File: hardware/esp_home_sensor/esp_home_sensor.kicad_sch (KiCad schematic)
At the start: 0 parts

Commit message: schematic
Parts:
- added BT1: Battery_Cell, symbol Device:Battery_Cell
- added J2, J3: Conn_01x04_MountingPin, Connector_JST:JST_SH_SM04B-SRSS-TB_1x04-1MP_P1.00mm_Horizontal, symbol Connector_Generic_MountingPin:Conn_01x04_MountingPin
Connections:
- new net 3V3_AUX: J2.3 (Pin_3), J3.3 (Pin_3)
- new net Env_sensor/SCL: J2.1 (Pin_1), J3.1 (Pin_1)
- new net Env_sensor/SDA: J2.2 (Pin_2), J3.2 (Pin_2)
- new net GND: J2.4 (Pin_4), J3.4 (Pin_4)
- new net Protection/BAT+: BT1.1 (+)
- new net Protection/BAT-: BT1.2 (-)
- no-connect marks 0 -> 2
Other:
- added sheet Charger (charger.kicad_sch)
- added sheet Env_sensor (env_sensor.kicad_sch)
- added sheet LDO (LDO.kicad_sch)
- added sheet Light_sensor (light_sensor.kicad_sch)
- added sheet MCU (MCU.kicad_sch)
- added sheet Protection (protection.kicad_sch)
- added sheet USB (USB.kicad_sch)

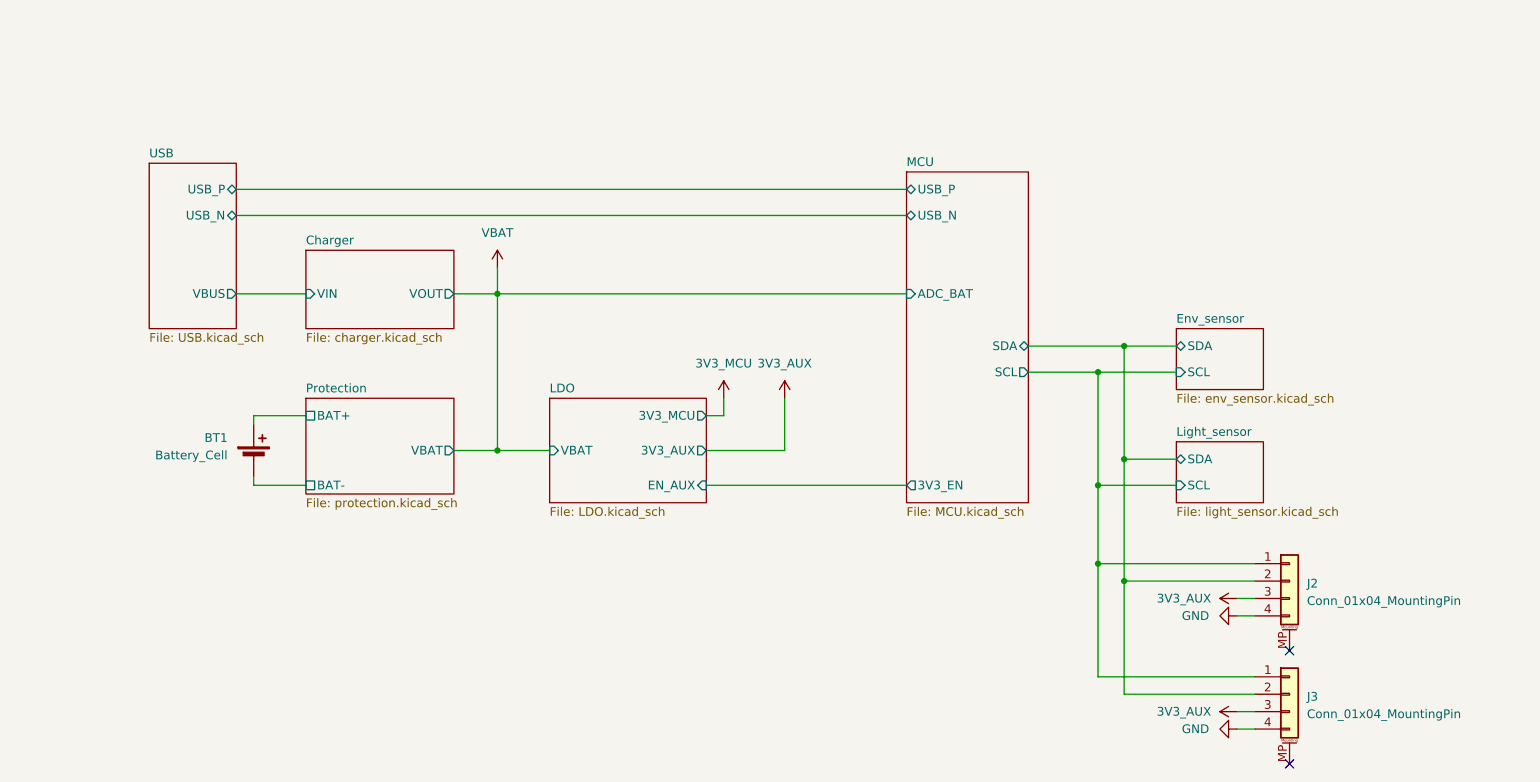
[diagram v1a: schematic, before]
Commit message: busses, display connector, footprint lib
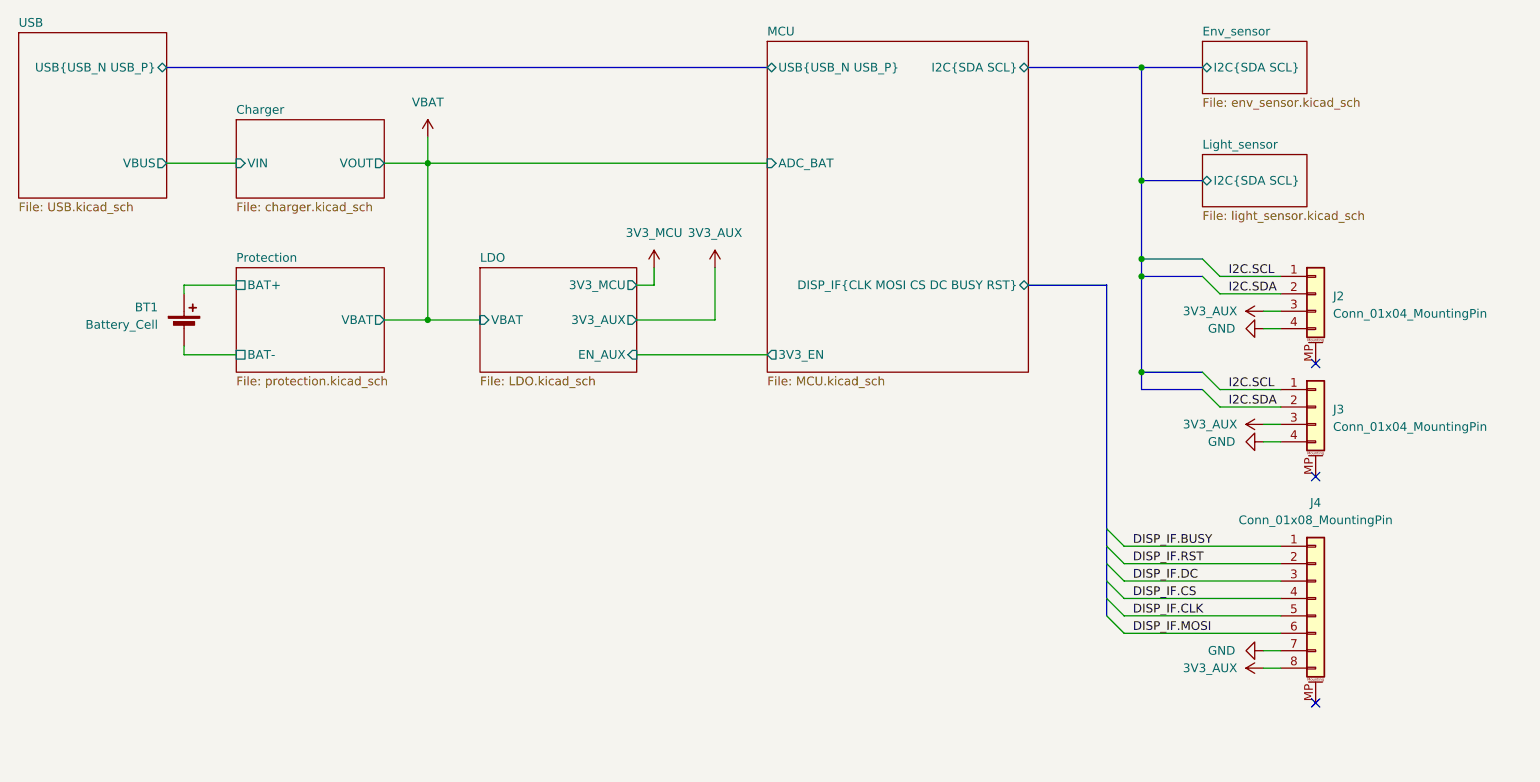
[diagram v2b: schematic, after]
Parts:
- added J4: Conn_01x08_MountingPin, Connector_JST:JST_SH_SM08B-SRSS-TB_1x08-1MP_P1.00mm_Horizontal, symbol Connector_Generic_MountingPin:Conn_01x08_MountingPin
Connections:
- net 3V3_AUX: now also J4.8 (Pin_8)
- net GND: now also J4.7 (Pin_7)
- net Env_sensor/SCL renamed I2C.SCL
- net Env_sensor/SDA renamed I2C.SDA
- new net DISP_IF.BUSY: J4.1 (Pin_1)
- new net DISP_IF.CLK: J4.5 (Pin_5)
- new net DISP_IF.CS: J4.4 (Pin_4)
- new net DISP_IF.DC: J4.3 (Pin_3)
- new net DISP_IF.MOSI: J4.6 (Pin_6)
- new net DISP_IF.RST: J4.2 (Pin_2)
- no-connect marks 2 -> 3
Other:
- sheet Env_sensor ports: added I2C{SDA SCL}; removed SCL, SDA
- sheet Light_sensor ports: added I2C{SDA SCL}; removed SCL, SDA
- sheet MCU ports: added DISP_IF{CLK MOSI CS DC BUSY RST}, I2C{SDA SCL}, USB{USB_N USB_P}; removed SCL, SDA, USB_N, USB_P
- sheet USB ports: added USB{USB_N USB_P}; removed USB_N, USB_P
- moved on the sheet: BT1, J2, J3

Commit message: footprint assignment, buck
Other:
- sheet LDO renamed DC_DC
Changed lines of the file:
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@@
+			)
+		)
+		(property "Mfr. No." ""
+			(at 218.44 99.06 0)
+			(hide yes)
+			(show_name no)
+			(do_not_autoplace no)
+			(effects
+				(font
+					(size 1.27 1.27)
+				)
 			)
 		)
@@
 			)
 		)
+		(property "Mfr. No." ""
+			(at 218.44 82.55 0)
+			(hide yes)
+			(show_name no)
+			(do_not_autoplace no)
+			(effects
+				(font
+					(size 1.27 1.27)
+				)
+			)
+		)
 		(pin "MP"
 		)
@@
 			)
 		)
+		(property "Mfr. No." ""
+			(at 53.34 87.63 0)
+			(hide yes)
+			(show_name no)
+			(do_not_autoplace no)
+			(effects
+				(font
+					(size 1.27 1.27)
+				)
+			)
+		)
 		(pin "1"
 		)
@@
 			)
 		)
+		(property "Mfr. No." ""
+			(at 218.44 127 0)
+			(hide yes)
+			(show_name no)
+			(do_not_autoplace no)
+			(effects
+				(font
+					(size 1.27 1.27)
+				)
+			)
+		)
 		(pin "7"
 		)
@@
 			(color 0 0 0 0)
 		)
-		(property "Sheetname" "LDO"
+		(property "Sheetname" "DC_DC"
 			(at 96.52 78.0284 0)
 			(show_name no)

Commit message: minor update
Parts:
- BT1: footprint (none) -> Battery:BatteryHolder_Keystone_1042_1x18650
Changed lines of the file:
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@@
 			)
 		)
-		(property "Footprint" ""
+		(property "Footprint" "Battery:BatteryHolder_Keystone_1042_1x18650"
 			(at 53.34 86.106 90)
 			(hide yes)

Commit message: initial layout, power routing
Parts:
- added H1, H2, H3, H4: MountingHole, MountingHole:MountingHole_2.2mm_M2, symbol Mechanical:MountingHole
- added R18: 100, Resistor_SMD:R_0402_1005Metric, symbol Device:R
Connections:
- net VBAT: now also R18.2
- new net MCU/ADC_BAT: R18.1

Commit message: layout
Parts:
- added TP24, TP25, TP27, TP28, TP29, TP30: TestPoint, TestPoint:TestPoint_Pad_D2.5mm, symbol Connector:TestPoint
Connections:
- net 3V3_AUX: now also TP25.1
- net 3V3_MCU: now also TP27.1
- net GND: now also TP24.1, TP29.1, TP30.1
- net VBAT: now also TP28.1

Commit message: layout
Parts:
- renumbered J2 to J1, J3 to J2, J4 to J3, R18 to R1, TP28 to TP1, TP30 to TP2, TP27 to TP3, TP29 to TP4, TP25 to TP5, TP24 to TP6
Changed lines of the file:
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@@
 		(dnp no)
 		(fields_autoplaced yes)
-		(property "Reference" "#PWR021"
+		(property "Reference" "#PWR02"
 			(at 88.9 63.5 0)
 			(hide yes)
@@
 			(project "esp_home_sensor"
 				(path "/1b1bee14-8d82-405b-b99d-415549a137e6"
-					(reference "#PWR021")
+					(reference "#PWR02")
 					(unit 1)
 				)
@@
 		(dnp no)
 		(fields_autoplaced yes)
-		(property "Reference" "J3"
+		(property "Reference" "J2"
 			(at 220.98 99.4155 0)
 			(show_name no)
@@
 			(project "esp_home_sensor"
 				(path "/1b1bee14-8d82-405b-b99d-415549a137e6"
-					(reference "J3")
+					(reference "J2")
 					(unit 1)
 				)
@@
 		(in_pos_files yes)
 		(dnp no)
-		(property "Reference" "TP24"
+		(property "Reference" "TP6"
 			(at 120.65 137.16 90)
 			(show_name no)
@@
 			(project "esp_home_sensor"
 				(path "/1b1bee14-8d82-405b-b99d-415549a137e6"
-					(reference "TP24")
+					(reference "TP6")
 					(unit 1)
 				)
@@
 		(dnp no)
 		(fields_autoplaced yes)
-		(property "Reference" "#PWR016"
+		(property "Reference" "#PWR09"
 			(at 121.92 82.55 0)
 			(hide yes)
@@
 			(project "esp_home_sensor"
 				(path "/1b1bee14-8d82-405b-b99d-415549a137e6"
-					(reference "#PWR016")
+					(reference "#PWR09")
 					(unit 1)
 				)
@@
 		(dnp no)
 		(fields_autoplaced yes)
-		(property "Reference" "#PWR047"
+		(property "Reference" "#PWR016"
 			(at 214.63 137.16 0)
 			(hide yes)
@@
 			(project "esp_home_sensor"
 				(path "/1b1bee14-8d82-405b-b99d-415549a137e6"
-					(reference "#PWR047")
+					(reference "#PWR016")
 					(unit 1)
 				)
@@
 		(in_pos_files yes)
 		(dnp no)
-		(property "Reference" "TP27"
+		(property "Reference" "TP3"
 			(at 120.65 125.73 90)
 			(show_name no)
@@
 			(project "esp_home_sensor"
 				(path "/1b1bee14-8d82-405b-b99d-415549a137e6"
-					(reference "TP27")
+					(reference "TP3")
 					(unit 1)
 				)
@@
 		(in_pos_files yes)
 		(dnp no)
-		(property "Reference" "#PWR044"
+		(property "Reference" "#PWR012"
 			(at 204.47 87.63 0)
 			(hide yes)
@@
 			(project "esp_home_sensor"
 				(path "/1b1bee14-8d82-405b-b99d-415549a137e6"
-					(reference "#PWR044")
+					(reference "#PWR012")
 					(unit 1)
 				)
@@
 		(in_pos_files yes)
 		(dnp no)
-		(property "Reference" "TP30"
+		(property "Reference" "TP2"
 			(at 120.65 120.65 90)
 			(show_name no)
@@
 			(project "esp_home_sensor"
 				(path "/1b1bee14-8d82-405b-b99d-415549a137e6"
-					(reference "TP30")
+					(reference "TP2")
 					(unit 1)
 				)
@@
 		(dnp no)
 		(fields_autoplaced yes)
-		(property "Reference" "#PWR043"
+		(property "Reference" "#PWR011"
 			(at 214.63 85.09 0)
 			(hide yes)
@@
 			(project "esp_home_sensor"
 				(path "/1b1bee14-8d82-405b-b99d-415549a137e6"
-					(reference "#PWR043")
+					(reference "#PWR011")
 					(unit 1)
 				)
@@
 		(dnp no)
 		(fields_autoplaced yes)
-		(property "Reference" "#PWR045"
+		(property "Reference" "#PWR013"
 			(at 214.63 101.6 0)
 			(hide yes)
@@
 			(project "esp_home_sensor"
 				(path "/1b1bee14-8d82-405b-b99d-415549a137e6"
-					(reference "#PWR045")
+					(reference "#PWR013")
 					(unit 1)
 				)
@@
 		(in_pos_files yes)
 		(dnp no)
-		(property "Reference" "R18"
+		(property "Reference" "R1"
 			(at 115.5701 60.96 0)
 			(show_name no)
@@
 			(project "esp_home_sensor"
 				(path "/1b1bee14-8d82-405b-b99d-415549a137e6"
-					(reference "R18")
+					(reference "R1")
 					(unit 1)
 				)
@@
 		(in_pos_files yes)
 		(dnp no)
-		(property "Reference" "#PWR060"
+		(property "Reference" "#PWR01"
 			(at 77.47 139.7 0)
 			(hide yes)
@@
 			(project "esp_home_sensor"
 				(path "/1b1bee14-8d82-405b-b99d-415549a137e6"
-					(reference "#PWR060")
+					(reference "#PWR01")
 					(unit 1)
 				)
@@
 		(in_pos_files yes)
 		(dnp no)
-		(property "Reference" "#PWR062"
+		(property "Reference" "#PWR03"
 			(at 106.68 120.65 0)
 			(hide yes)
@@
 			(project "esp_home_sensor"
 				(path "/1b1bee14-8d82-405b-b99d-415549a137e6"
-					(reference "#PWR062")
+					(reference "#PWR03")
 					(unit 1)
 				)
@@
 		(in_pos_files yes)
 		(dnp no)
-		(property "Reference" "#PWR048"
+		(property "Reference" "#PWR015"
 			(at 204.47 134.62 0)
 			(hide yes)
@@
 			(project "esp_home_sensor"
 				(path "/1b1bee14-8d82-405b-b99d-415549a137e6"
-					(reference "#PWR048")
+					(reference "#PWR015")
 					(unit 1)
 				)
@@
 		(dnp no)
 		(fields_autoplaced yes)
-		(property "Reference" "J2"
+		(property "Reference" "J1"
 			(at 220.98 82.9055 0)
 			(show_name no)
@@
 			(project "esp_home_sensor"
 				(path "/1b1bee14-8d82-405b-b99d-415549a137e6"
-					(reference "J2")
+					(reference "J1")
 					(unit 1)
 				)
@@
 		(dnp no)
 		(fields_autoplaced yes)
-		(property "Reference" "#PWR017"
+		(property "Reference" "#PWR010"
 			(at 130.81 82.55 0)
 			(hide yes)
@@
 			(project "esp_home_sensor"
 				(path "/1b1bee14-8d82-405b-b99d-415549a137e6"
-					(reference "#PWR017")
+					(reference "#PWR010")
 					(unit 1)
 				)
@@
 		(in_pos_files yes)
 		(dnp no)
-		(property "Reference" "#PWR059"
+		(property "Reference" "#PWR06"
 			(at 106.68 137.16 0)
 			(hide yes)
@@
 			(project "esp_home_sensor"
 				(path "/1b1bee14-8d82-405b-b99d-415549a137e6"
-					(reference "#PWR059")
+					(reference "#PWR06")
 					(unit 1)
 				)
@@
 		(in_pos_files yes)
 		(dnp no)
-		(property "Reference" "#PWR061"
+		(property "Reference" "#PWR04"
 			(at 106.68 128.27 0)
 			(hide yes)
@@
 			(project "esp_home_sensor"
 				(path "/1b1bee14-8d82-405b-b99d-415549a137e6"
-					(reference "#PWR061")
+					(reference "#PWR04")
 					(unit 1)
 				)
@@
 		(in_pos_files yes)
 		(dnp no)
-		(property "Reference" "#PWR046"
+		(property "Reference" "#PWR014"
 			(at 204.47 104.14 0)
 			(hide yes)
@@
 			(project "esp_home_sensor"
 				(path "/1b1bee14-8d82-405b-b99d-415549a137e6"
-					(reference "#PWR046")
+					(reference "#PWR014")
 					(unit 1)
 				)
@@
 		(dnp no)
 		(fields_autoplaced yes)
-		(property "Reference" "#PWR063"
+		(property "Reference" "#PWR05"
 			(at 116.84 134.62 0)
 			(hide yes)
@@
 			(project "esp_home_sensor"
 				(path "/1b1bee14-8d82-405b-b99d-415549a137e6"
-					(reference "#PWR063")
+					(reference "#PWR05")
 					(unit 1)
 				)
@@
 		(in_pos_files yes)
 		(dnp no)
-		(property "Reference" "TP25"
+		(property "Reference" "TP5"
 			(at 120.65 134.62 90)
 			(show_name no)
@@
 			(project "esp_home_sensor"
 				(path "/1b1bee14-8d82-405b-b99d-415549a137e6"
-					(reference "TP25")
+					(reference "TP5")
 					(unit 1)
 				)
@@
 		(in_pos_files yes)
 		(dnp no)
-		(property "Reference" "TP29"
+		(property "Reference" "TP4"
 			(at 120.65 128.27 90)
 			(show_name no)
@@
 			(project "esp_home_sensor"
 				(path "/1b1bee14-8d82-405b-b99d-415549a137e6"
-					(reference "TP29")
+					(reference "TP4")
 					(unit 1)
 				)
@@
 		(in_pos_files yes)
 		(dnp no)
-		(property "Reference" "TP28"
+		(property "Reference" "TP1"
 			(at 120.65 118.11 90)
 			(show_name no)
@@
 			(project "esp_home_sensor"
 				(path "/1b1bee14-8d82-405b-b99d-415549a137e6"
-					(reference "TP28")
+					(reference "TP1")
 					(unit 1)
 				)
@@
 		(dnp no)
 		(fields_autoplaced yes)
-		(property "Reference" "#PWR033"
+		(property "Reference" "#PWR08"
 			(at 118.11 125.73 0)
 			(hide yes)
@@
 			(project "esp_home_sensor"
 				(path "/1b1bee14-8d82-405b-b99d-415549a137e6"
-					(reference "#PWR033")
+					(reference "#PWR08")
 					(unit 1)
 				)
@@
 		(in_pos_files yes)
 		(dnp no)
-		(property "Reference" "J4"
+		(property "Reference" "J3"
 			(at 218.44 113.03 0)
 			(show_name no)
@@
 			(project "esp_home_sensor"
 				(path "/1b1bee14-8d82-405b-b99d-415549a137e6"
-					(reference "J4")
+					(reference "J3")
 					(unit 1)
 				)
@@
 		(dnp no)
 		(fields_autoplaced yes)
-		(property "Reference" "#PWR034"
+		(property "Reference" "#PWR07"
 			(at 118.11 118.11 0)
 			(hide yes)
@@
 			(project "esp_home_sensor"
 				(path "/1b1bee14-8d82-405b-b99d-415549a137e6"
-					(reference "#PWR034")
-					(unit 1)
-				)
+					(reference "#PWR07")
+					(unit 1)
+				)

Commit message: in production
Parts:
- BT1: footprint Battery:BatteryHolder_Keystone_1042_1x18650 -> (none); Mfr. No. (none) -> BH-18650-B6AA002
- J1, J2, J3, TP1, TP2, TP3, TP4, TP5, TP6: now left out of the parts list
- R1: Mfr. No. (none) -> RT0402DRE07100RL
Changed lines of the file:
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@@
 		(body_style 1)
 		(exclude_from_sim no)
-		(in_bom yes)
+		(in_bom no)
 		(on_board yes)
 		(in_pos_files yes)
@@
 		(body_style 1)
 		(exclude_from_sim no)
-		(in_bom yes)
+		(in_bom no)
 		(on_board yes)
 		(in_pos_files yes)
@@
 		(body_style 1)
 		(exclude_from_sim no)
-		(in_bom yes)
+		(in_bom no)
 		(on_board yes)
 		(in_pos_files yes)
@@
 		(body_style 1)
 		(exclude_from_sim no)
-		(in_bom yes)
+		(in_bom no)
 		(on_board yes)
 		(in_pos_files yes)
@@
 			)
 		)
-		(property "Mfr. No." ""
+		(property "Mfr. No." "RT0402DRE07100RL"
 			(at 114.3 63.5 0)
 			(hide yes)
@@
 		(body_style 1)
 		(exclude_from_sim no)
-		(in_bom yes)
+		(in_bom no)
 		(on_board yes)
 		(in_pos_files yes)
@@
 			)
 		)
-		(property "Footprint" "Battery:BatteryHolder_Keystone_1042_1x18650"
+		(property "Footprint" ""
 			(at 53.34 86.106 90)
 			(hide yes)
@@
 			)
 		)
-		(property "Mfr. No." ""
+		(property "Mfr. No." "BH-18650-B6AA002"
 			(at 53.34 87.63 0)
 			(hide yes)
@@
 		(body_style 1)
 		(exclude_from_sim no)
-		(in_bom yes)
+		(in_bom no)
 		(on_board yes)
 		(in_pos_files yes)
@@
 		(body_style 1)
 		(exclude_from_sim no)
-		(in_bom yes)
+		(in_bom no)
 		(on_board yes)
 		(in_pos_files yes)
@@
 		(body_style 1)
 		(exclude_from_sim no)
-		(in_bom yes)
+		(in_bom no)
 		(on_board yes)
 		(in_pos_files yes)
@@
 		(body_style 1)
 		(exclude_from_sim no)
-		(in_bom yes)
-		(on_board yes)
-		(in_pos_files yes)
+		(in_bom no)
+		(on_board yes)
+		(in_pos_files yes)
